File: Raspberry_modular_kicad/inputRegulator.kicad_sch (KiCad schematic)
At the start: 4 parts

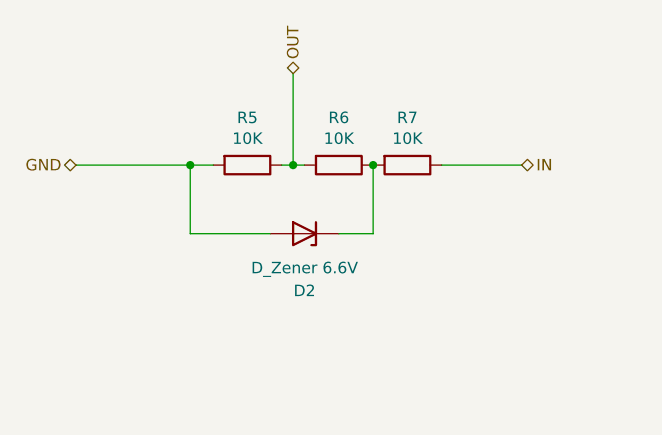
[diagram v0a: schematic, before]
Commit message: [UDPT] All symbols are now in lib
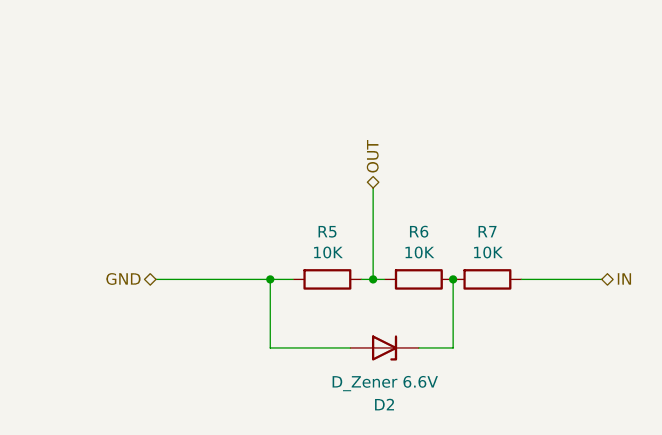
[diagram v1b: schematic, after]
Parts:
- D2: symbol Device:D_Zener -> Modular Shield:D_Zener
- R5, R6, R7: symbol Device:R -> Modular Shield:R
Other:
- moved on the sheet: D2, R5, R6, R7
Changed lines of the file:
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@@
 (kicad_sch (version 20230121) (generator eeschema)
   (paper "A4")
-  (junction (at 24.13 17.78) (diameter 0) (color 0 0 0 0)
-  )
-  (junction (at 44.45 17.78) (diameter 0) (color 0 0 0 0)
-  )
-  (junction (at 35.56 17.78) (diameter 0) (color 0 0 0 0)
-  )
-  (wire (pts (xy 34.29 17.78) (xy 35.56 17.78))
-    (stroke (width 0) (type default))
-  )
-  (wire (pts (xy 24.13 17.78) (xy 26.67 17.78))
-    (stroke (width 0) (type default))
-  )
-  (wire (pts (xy 44.45 25.4) (xy 44.45 17.78))
-    (stroke (width 0) (type default))
-  )
-  (wire (pts (xy 24.13 25.4) (xy 24.13 17.78))
-    (stroke (width 0) (type default))
-  )
-  (wire (pts (xy 35.56 17.78) (xy 36.83 17.78))
-    (stroke (width 0) (type default))
-  )
-  (wire (pts (xy 11.43 17.78) (xy 24.13 17.78))
-    (stroke (width 0) (type default))
-  )
-  (wire (pts (xy 33.02 25.4) (xy 24.13 25.4))
-    (stroke (width 0) (type default))
-  )
-  (wire (pts (xy 35.56 7.62) (xy 35.56 17.78))
-    (stroke (width 0) (type default))
-  )
-  (wire (pts (xy 40.64 25.4) (xy 44.45 25.4))
-    (stroke (width 0) (type default))
-  )
-  (wire (pts (xy 52.07 17.78) (xy 60.96 17.78))
-    (stroke (width 0) (type default))
-  )
-  (hierarchical_label "OUT" (shape bidirectional) (at 35.56 7.62 90)
+  (junction (at 33.02 30.48) (diameter 0) (color 0 0 0 0)
+  )
+  (junction (at 53.34 30.48) (diameter 0) (color 0 0 0 0)
+  )
+  (junction (at 44.45 30.48) (diameter 0) (color 0 0 0 0)
+  )
+  (wire (pts (xy 43.18 30.48) (xy 44.45 30.48))
+    (stroke (width 0) (type default))
+  )
+  (wire (pts (xy 33.02 30.48) (xy 35.56 30.48))
+    (stroke (width 0) (type default))
+  )
+  (wire (pts (xy 53.34 38.1) (xy 53.34 30.48))
+    (stroke (width 0) (type default))
+  )
+  (wire (pts (xy 33.02 38.1) (xy 33.02 30.48))
+    (stroke (width 0) (type default))
+  )
+  (wire (pts (xy 44.45 30.48) (xy 45.72 30.48))
+    (stroke (width 0) (type default))
+  )
+  (wire (pts (xy 20.32 30.48) (xy 33.02 30.48))
+    (stroke (width 0) (type default))
+  )
+  (wire (pts (xy 41.91 38.1) (xy 33.02 38.1))
+    (stroke (width 0) (type default))
+  )
+  (wire (pts (xy 44.45 20.32) (xy 44.45 30.48))
+    (stroke (width 0) (type default))
+  )
+  (wire (pts (xy 49.53 38.1) (xy 53.34 38.1))
+    (stroke (width 0) (type default))
+  )
+  (wire (pts (xy 60.96 30.48) (xy 69.85 30.48))
+    (stroke (width 0) (type default))
+  )
+  (hierarchical_label "OUT" (shape bidirectional) (at 44.45 20.32 90)
     (effects (font (size 1.27 1.27)) (justify left))
   )
-  (hierarchical_label "IN" (shape bidirectional) (at 60.96 17.78 0)
+  (hierarchical_label "IN" (shape bidirectional) (at 69.85 30.48 0)
     (effects (font (size 1.27 1.27)) (justify left))
   )
-  (hierarchical_label "GND" (shape bidirectional) (at 11.43 17.78 180)
+  (hierarchical_label "GND" (shape bidirectional) (at 20.32 30.48 180)
     (effects (font (size 1.27 1.27)) (justify right))
   )
-  (symbol (lib_id "Device:R") (at 40.64 17.78 270) (unit 1)
-    (in_bom yes) (on_board yes) (dnp no)
-    (property "Reference" "R6" (at 40.64 12.5222 90)
-      (effects (font (size 1.27 1.27)))
-    )
-    (property "Value" "10K" (at 40.64 14.8336 90)
-      (effects (font (size 1.27 1.27)))
-    )
-    (property "Footprint" "Raspberry_modular:R_0603_1608Metric" (at 40.64 16.002 90)
-      (effects (font (size 1.27 1.27)) hide)
-    )
-    (property "Datasheet" "~" (at 40.64 17.78 0)
+  (symbol (lib_id "Modular Shield:R") (at 49.53 30.48 270) (unit 1)
+    (in_bom yes) (on_board yes) (dnp no)
+    (property "Reference" "R6" (at 49.53 25.2222 90)
+      (effects (font (size 1.27 1.27)))
+    )
+    (property "Value" "10K" (at 49.53 27.5336 90)
+      (effects (font (size 1.27 1.27)))
+    )
+    (property "Footprint" "Raspberry_modular:R_0603_1608Metric" (at 49.53 28.702 90)
+      (effects (font (size 1.27 1.27)) hide)
+    )
+    (property "Datasheet" "~" (at 49.53 30.48 0)
       (effects (font (size 1.27 1.27)) hide)
     )
@@
     )
   )
-  (symbol (lib_id "Device:R") (at 48.26 17.78 270) (unit 1)
-    (in_bom yes) (on_board yes) (dnp no)
-    (property "Reference" "R7" (at 48.26 12.5222 90)
-      (effects (font (size 1.27 1.27)))
-    )
-    (property "Value" "10K" (at 48.26 14.8336 90)
-      (effects (font (size 1.27 1.27)))
-    )
-    (property "Footprint" "Raspberry_modular:R_0603_1608Metric" (at 48.26 16.002 90)
-      (effects (font (size 1.27 1.27)) hide)
-    )
-    (property "Datasheet" "~" (at 48.26 17.78 0)
+  (symbol (lib_id "Modular Shield:R") (at 57.15 30.48 270) (unit 1)
+    (in_bom yes) (on_board yes) (dnp no)
+    (property "Reference" "R7" (at 57.15 25.2222 90)
+      (effects (font (size 1.27 1.27)))
+    )
+    (property "Value" "10K" (at 57.15 27.5336 90)
+      (effects (font (size 1.27 1.27)))
+    )
+    (property "Footprint" "Raspberry_modular:R_0603_1608Metric" (at 57.15 28.702 90)
+      (effects (font (size 1.27 1.27)) hide)
+    )
+    (property "Datasheet" "~" (at 57.15 30.48 0)
       (effects (font (size 1.27 1.27)) hide)
     )
@@
     )
   )
-  (symbol (lib_id "Device:R") (at 30.48 17.78 270) (unit 1)
-    (in_bom yes) (on_board yes) (dnp no)
-    (property "Reference" "R5" (at 30.48 12.5222 90)
-      (effects (font (size 1.27 1.27)))
-    )
-    (property "Value" "10K" (at 30.48 14.8336 90)
-      (effects (font (size 1.27 1.27)))
-    )
-    (property "Footprint" "Raspberry_modular:R_0603_1608Metric" (at 30.48 16.002 90)
-      (effects (font (size 1.27 1.27)) hide)
-    )
-    (property "Datasheet" "~" (at 30.48 17.78 0)
+  (symbol (lib_id "Modular Shield:R") (at 39.37 30.48 270) (unit 1)
+    (in_bom yes) (on_board yes) (dnp no)
+    (property "Reference" "R5" (at 39.37 25.2222 90)
+      (effects (font (size 1.27 1.27)))
+    )
+    (property "Value" "10K" (at 39.37 27.5336 90)
+      (effects (font (size 1.27 1.27)))
+    )
+    (property "Footprint" "Raspberry_modular:R_0603_1608Metric" (at 39.37 28.702 90)
+      (effects (font (size 1.27 1.27)) hide)
+    )
+    (property "Datasheet" "~" (at 39.37 30.48 0)
       (effects (font (size 1.27 1.27)) hide)
     )
@@
     )
   )
-  (symbol (lib_id "Device:D_Zener") (at 36.83 25.4 180) (unit 1)
-    (in_bom yes) (on_board yes) (dnp no)
-    (property "Reference" "D2" (at 36.83 31.75 0)
-      (effects (font (size 1.27 1.27)))
-    )
-    (property "Value" "D_Zener 6.6V" (at 36.83 29.21 0)
-      (effects (font (size 1.27 1.27)))
-    )
-    (property "Footprint" "Raspberry_modular:D_0603_1608Metric" (at 36.83 25.4 0)
-      (effects (font (size 1.27 1.27)) hide)
-    )
-    (property "Datasheet" "~" (at 36.83 25.4 0)
-      (effects (font (size 1.27 1.27)) hide)
-    )
+  (symbol (lib_id "Modular Shield:D_Zener") (at 45.72 38.1 180) (unit 1)
+    (in_bom yes) (on_board yes) (dnp no)
+    (property "Reference" "D2" (at 45.72 44.45 0)
+      (effects (font (size 1.27 1.27)))
+    )
+    (property "Value" "D_Zener 6.6V" (at 45.72 41.91 0)
+      (effects (font (size 1.27 1.27)))
+    )
+    (property "Footprint" "Raspberry_modular:D_0603_1608Metric" (at 45.72 38.1 0)
+      (effects (font (size 1.27 1.27)) hide)
+    )
+    (property "Datasheet" "~" (at 45.72 38.1 0)
+      (effects (font (size 1.27 1.27)) hide)
+    )

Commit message: [UDPT] Inputs on schematics
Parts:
- renumbered D2 to D3, R7 to R10, R5 to R8, R6 to R9
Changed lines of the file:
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@@
     (stroke (width 0) (type default))
   )
-  (hierarchical_label "OUT" (shape bidirectional) (at 44.45 20.32 90)
+  (hierarchical_label "OUT" (shape bidirectional) (at 44.45 20.32 90) (fields_autoplaced)
     (effects (font (size 1.27 1.27)) (justify left))
   )
-  (hierarchical_label "IN" (shape bidirectional) (at 69.85 30.48 0)
+  (hierarchical_label "IN" (shape bidirectional) (at 69.85 30.48 0) (fields_autoplaced)
     (effects (font (size 1.27 1.27)) (justify left))
   )
-  (hierarchical_label "GND" (shape bidirectional) (at 20.32 30.48 180)
+  (hierarchical_label "GND" (shape bidirectional) (at 20.32 30.48 180) (fields_autoplaced)
     (effects (font (size 1.27 1.27)) (justify right))
   )
   (symbol (lib_id "Modular Shield:R") (at 49.53 30.48 270) (unit 1)
     (in_bom yes) (on_board yes) (dnp no)
-    (property "Reference" "R6" (at 49.53 25.2222 90)
+    (property "Reference" "R9" (at 49.53 25.2222 90)
       (effects (font (size 1.27 1.27)))
     )
@@
   (symbol (lib_id "Modular Shield:R") (at 57.15 30.48 270) (unit 1)
     (in_bom yes) (on_board yes) (dnp no)
-    (property "Reference" "R7" (at 57.15 25.2222 90)
+    (property "Reference" "R10" (at 57.15 25.2222 90)
       (effects (font (size 1.27 1.27)))
     )
@@
   (symbol (lib_id "Modular Shield:R") (at 39.37 30.48 270) (unit 1)
     (in_bom yes) (on_board yes) (dnp no)
-    (property "Reference" "R5" (at 39.37 25.2222 90)
+    (property "Reference" "R8" (at 39.37 25.2222 90)
       (effects (font (size 1.27 1.27)))
     )
@@
   (symbol (lib_id "Modular Shield:D_Zener") (at 45.72 38.1 180) (unit 1)
     (in_bom yes) (on_board yes) (dnp no)
-    (property "Reference" "D2" (at 45.72 44.45 0)
-      (effects (font (size 1.27 1.27)))
-    )
+    (property "Reference" "D3" (at 45.72 44.45 0)
+      (effects (font (size 1.27 1.27)))
+    )

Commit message: [UDPT] Shematics
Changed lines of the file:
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@@
   (symbol (lib_id "Modular Shield:R") (at 49.53 30.48 270) (unit 1)
     (in_bom yes) (on_board yes) (dnp no)
-    (property "Reference" "R9" (at 49.53 25.2222 90)
+    (property "Reference" "R9" (at 49.53 27.94 90)
       (effects (font (size 1.27 1.27)))
     )
-    (property "Value" "10K" (at 49.53 27.5336 90)
+    (property "Value" "10K" (at 49.53 30.48 90)
       (effects (font (size 1.27 1.27)))
     )
@@
   (symbol (lib_id "Modular Shield:R") (at 57.15 30.48 270) (unit 1)
     (in_bom yes) (on_board yes) (dnp no)
-    (property "Reference" "R10" (at 57.15 25.2222 90)
+    (property "Reference" "R10" (at 57.15 27.94 90)
       (effects (font (size 1.27 1.27)))
     )
-    (property "Value" "10K" (at 57.15 27.5336 90)
+    (property "Value" "10K" (at 57.15 30.48 90)
       (effects (font (size 1.27 1.27)))
     )
@@
   (symbol (lib_id "Modular Shield:R") (at 39.37 30.48 270) (unit 1)
     (in_bom yes) (on_board yes) (dnp no)
-    (property "Reference" "R8" (at 39.37 25.2222 90)
+    (property "Reference" "R8" (at 39.37 27.94 90)
       (effects (font (size 1.27 1.27)))
     )
-    (property "Value" "10K" (at 39.37 27.5336 90)
+    (property "Value" "10K" (at 39.37 30.48 90)
       (effects (font (size 1.27 1.27)))
     )

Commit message: [UDPT] Electricals footprints
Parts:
- D3: footprint Raspberry_modular:D_0603_1608Metric -> Modular Shield:D_0603_1608Metric
- R10, R8, R9: footprint Raspberry_modular:R_0603_1608Metric -> Modular Shield:R_0603_1608Metric
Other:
- moved on the sheet: D3, R10
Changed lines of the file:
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@@
   (junction (at 33.02 30.48) (diameter 0) (color 0 0 0 0)
   )
-  (junction (at 53.34 30.48) (diameter 0) (color 0 0 0 0)
+  (junction (at 54.61 30.48) (diameter 0) (color 0 0 0 0)
   )
   (junction (at 44.45 30.48) (diameter 0) (color 0 0 0 0)
@@
     (stroke (width 0) (type default))
   )
-  (wire (pts (xy 53.34 38.1) (xy 53.34 30.48))
+  (wire (pts (xy 54.61 38.1) (xy 54.61 30.48))
+    (stroke (width 0) (type default))
+  )
+  (wire (pts (xy 54.61 30.48) (xy 53.34 30.48))
     (stroke (width 0) (type default))
   )
@@
     (stroke (width 0) (type default))
   )
+  (wire (pts (xy 55.88 30.48) (xy 54.61 30.48))
+    (stroke (width 0) (type default))
+  )
   (wire (pts (xy 20.32 30.48) (xy 33.02 30.48))
     (stroke (width 0) (type default))
   )
-  (wire (pts (xy 41.91 38.1) (xy 33.02 38.1))
+  (wire (pts (xy 40.64 38.1) (xy 33.02 38.1))
     (stroke (width 0) (type default))
   )
@@
     (stroke (width 0) (type default))
   )
-  (wire (pts (xy 49.53 38.1) (xy 53.34 38.1))
-    (stroke (width 0) (type default))
-  )
-  (wire (pts (xy 60.96 30.48) (xy 69.85 30.48))
+  (wire (pts (xy 48.26 38.1) (xy 54.61 38.1))
+    (stroke (width 0) (type default))
+  )
+  (wire (pts (xy 63.5 30.48) (xy 69.85 30.48))
     (stroke (width 0) (type default))
   )
@@
       (effects (font (size 1.27 1.27)))
     )
-    (property "Footprint" "Raspberry_modular:R_0603_1608Metric" (at 49.53 28.702 90)
+    (property "Footprint" "Modular Shield:R_0603_1608Metric" (at 49.53 28.702 90)
       (effects (font (size 1.27 1.27)) hide)
     )
@@
     )
   )
-  (symbol (lib_id "Modular Shield:R") (at 57.15 30.48 270) (unit 1)
-    (in_bom yes) (on_board yes) (dnp no)
-    (property "Reference" "R10" (at 57.15 27.94 90)
-      (effects (font (size 1.27 1.27)))
-    )
-    (property "Value" "10K" (at 57.15 30.48 90)
-      (effects (font (size 1.27 1.27)))
-    )
-    (property "Footprint" "Raspberry_modular:R_0603_1608Metric" (at 57.15 28.702 90)
-      (effects (font (size 1.27 1.27)) hide)
-    )
-    (property "Datasheet" "~" (at 57.15 30.48 0)
+  (symbol (lib_id "Modular Shield:R") (at 59.69 30.48 270) (unit 1)
+    (in_bom yes) (on_board yes) (dnp no)
+    (property "Reference" "R10" (at 59.69 27.94 90)
+      (effects (font (size 1.27 1.27)))
+    )
+    (property "Value" "10K" (at 59.69 30.48 90)
+      (effects (font (size 1.27 1.27)))
+    )
+    (property "Footprint" "Modular Shield:R_0603_1608Metric" (at 59.69 28.702 90)
+      (effects (font (size 1.27 1.27)) hide)
+    )
+    (property "Datasheet" "~" (at 59.69 30.48 0)
       (effects (font (size 1.27 1.27)) hide)
     )
@@
       (effects (font (size 1.27 1.27)))
     )
-    (property "Footprint" "Raspberry_modular:R_0603_1608Metric" (at 39.37 28.702 90)
+    (property "Footprint" "Modular Shield:R_0603_1608Metric" (at 39.37 28.702 90)
       (effects (font (size 1.27 1.27)) hide)
     )
@@
     )
   )
-  (symbol (lib_id "Modular Shield:D_Zener") (at 45.72 38.1 180) (unit 1)
-    (in_bom yes) (on_board yes) (dnp no)
-    (property "Reference" "D3" (at 45.72 44.45 0)
-      (effects (font (size 1.27 1.27)))
-    )
-    (property "Value" "D_Zener 6.6V" (at 45.72 41.91 0)
-      (effects (font (size 1.27 1.27)))
-    )
-    (property "Footprint" "Raspberry_modular:D_0603_1608Metric" (at 45.72 38.1 0)
-      (effects (font (size 1.27 1.27)) hide)
-    )
-    (property "Datasheet" "~" (at 45.72 38.1 0)
-      (effects (font (size 1.27 1.27)) hide)
-    )
+  (symbol (lib_id "Modular Shield:D_Zener") (at 44.45 38.1 180) (unit 1)
+    (in_bom yes) (on_board yes) (dnp no)
+    (property "Reference" "D3" (at 44.45 44.45 0)
+      (effects (font (size 1.27 1.27)))
+    )
+    (property "Value" "D_Zener 6.6V" (at 44.45 41.91 0)
+      (effects (font (size 1.27 1.27)))
+    )
+    (property "Footprint" "Modular Shield:D_0603_1608Metric" (at 44.45 38.1 0)
+      (effects (font (size 1.27 1.27)) hide)
+    )
+    (property "Datasheet" "~" (at 44.45 38.1 0)
+      (effects (font (size 1.27 1.27)) hide)
+    )

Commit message: [ADD] Bom
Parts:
- D3: LCSC (none) -> C894569
- R10, R8, R9: LCSC (none) -> C25804
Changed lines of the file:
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@@
+      (effects (font (size 1.27 1.27)) hide)
+    )
+    (property "LCSC" "C25804" (at 49.53 34.29 90)
       (effects (font (size 1.27 1.27)) hide)
     )
@@
       (effects (font (size 1.27 1.27)) hide)
     )
+    (property "LCSC" "C25804" (at 59.69 34.29 90)
+      (effects (font (size 1.27 1.27)) hide)
+    )
     (pin "1")
     (pin "2")
@@
       (effects (font (size 1.27 1.27)) hide)
     )
+    (property "LCSC" "C25804" (at 39.37 34.29 90)
+      (effects (font (size 1.27 1.27)) hide)
+    )
     (pin "1")
     (pin "2")
@@
       (effects (font (size 1.27 1.27)) hide)
     )
+    (property "LCSC" "C894569" (at 44.45 44.45 0)
+      (effects (font (size 1.27 1.27)) hide)
+    )
